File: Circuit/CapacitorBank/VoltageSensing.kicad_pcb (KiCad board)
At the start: 2 copper layers, 48.3 x 22.9 mm, 12 parts, among them J1 From Capacitor Bank, J2 To Control, U1 VTL5C, U2 VTL5C, U3 LM358

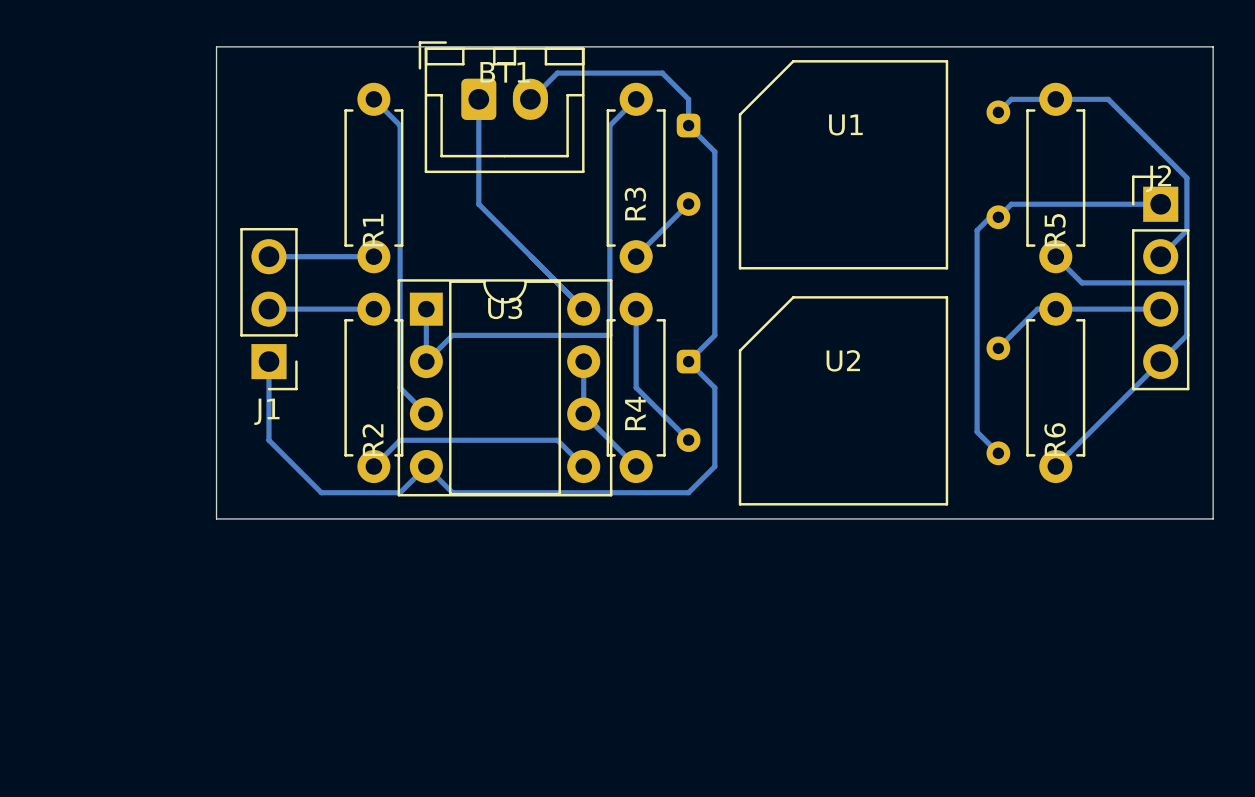
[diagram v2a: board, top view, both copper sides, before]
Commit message: [Circuit] One channel voltage sensing and control modules
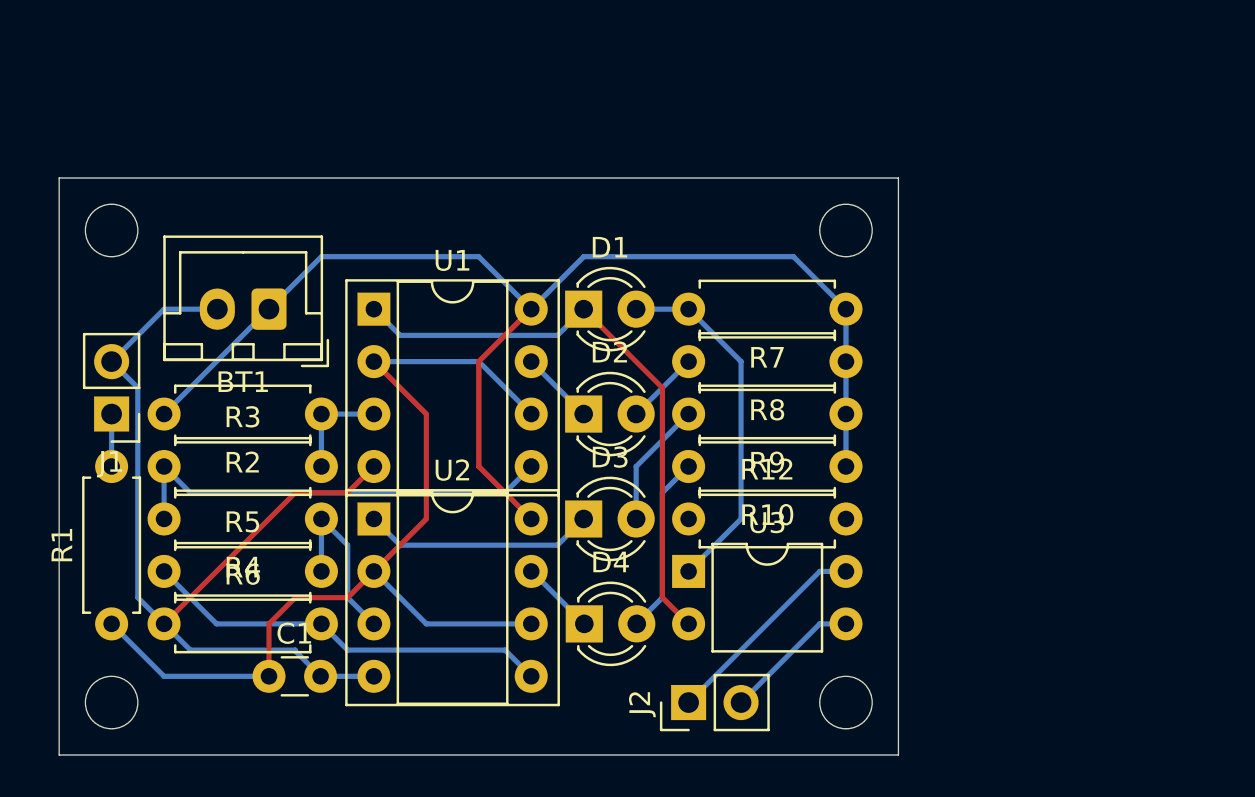
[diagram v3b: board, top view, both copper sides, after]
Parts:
- added C1: 0.1uF, Capacitor_THT:C_Disc_D3.0mm_W1.6mm_P2.50mm, F.Cu at (71.1, 73.7)
- added D1: LED, LED_THT:LED_D3.0mm_FlatTop, F.Cu at (86.4, 55.9)
- added D2: LED, LED_THT:LED_D3.0mm_FlatTop, F.Cu at (86.4, 61.0)
- added D3: LED, LED_THT:LED_D3.0mm_FlatTop, F.Cu at (86.4, 66.0)
- added D4: LED, LED_THT:LED_D3.0mm_FlatTop, F.Cu at (86.4, 71.1)
- added R10: 1K, Resistor_THT:R_Axial_DIN0207_L6.3mm_D2.5mm_P7.62mm_Horizontal, F.Cu at (99.1, 63.5)
- added R12: 1K, Resistor_THT:R_Axial_DIN0207_L6.3mm_D2.5mm_P7.62mm_Horizontal, F.Cu at (91.4, 66.0)
- added R7: 510, Resistor_THT:R_Axial_DIN0207_L6.3mm_D2.5mm_P7.62mm_Horizontal, F.Cu at (99.1, 55.9)
- added R8: 1K, Resistor_THT:R_Axial_DIN0207_L6.3mm_D2.5mm_P7.62mm_Horizontal, F.Cu at (99.1, 58.4)
- added R9: 1K, Resistor_THT:R_Axial_DIN0207_L6.3mm_D2.5mm_P7.62mm_Horizontal, F.Cu at (99.1, 61.0)
- J1: footprint Connector_PinHeader_2.54mm:PinHeader_1x03_P2.54mm_Vertical -> Connector_PinHeader_2.54mm:PinHeader_1x02_P2.54mm_Vertical
- J2: footprint Connector_PinHeader_2.54mm:PinHeader_1x04_P2.54mm_Vertical -> Connector_PinHeader_2.54mm:PinHeader_1x02_P2.54mm_Vertical
- R2: value 1K -> 6.8K
- R3: value 680 -> 5.1K
- R4: value 100 -> 5.1K
- R5, R6: value 4.7K -> 5.1K
- U1, U2: value VTL5C -> LM393; footprint OptoDevice:PerkinElmer_VTL5C -> Package_DIP:DIP-8_W7.62mm_Socket
- U3: value LM358 -> PC817; footprint Package_DIP:DIP-8_W7.62mm_Socket -> Package_DIP:DIP-4_W7.62mm
- moved R5 45.8 mm to (66.0, 68.6), turned to 0 degrees
- moved R6 43.8 mm to (66.0, 71.1), turned to 0 degrees
- moved J2 33.2 mm to (91.4, 74.9), turned to 90 degrees
- moved R1 28.4 mm to (63.5, 71.1), turned to 90 degrees
- moved R3 25.0 mm to (66.0, 63.5), turned to 0 degrees
- moved R4 18.3 mm to (73.7, 66.0), turned to 180 degrees
- moved U3 18.0 mm to (91.4, 68.6)
- moved U1 17.6 mm to (76.2, 55.9)
- moved U2 17.0 mm to (76.2, 66.0)
- moved BT1 14.4 mm to (71.1, 55.9), turned to 180 degrees
- moved J1 8.03 mm to (63.5, 61.0)
- moved R2 3.59 mm to (73.7, 61.0), turned to 180 degrees
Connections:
- J1 pad 1: GND -> /Sensor9V
- J1 pad 2: /Sensor3V -> GND
- J2 pad 1: /ControlPower+ -> /ControlSignal
- J2 pad 2: /ControlSignal1 -> /ControlGND
- R1 pad 1: Net-(R1-Pad1) -> Net-(C1-Pad1)
- R2 pad 2: /Sensor3V -> +12V
- R3 pad 2: Net-(R3-Pad2) -> Net-(R2-Pad1)
- R4 pad 2: Net-(R4-Pad2) -> Net-(R3-Pad1)
- R5 pad 1: /ControlPower- -> Net-(R5-Pad1)
- R5 pad 2: /ControlSignal1 -> Net-(R4-Pad1)
- R6 pad 1: /ControlPower- -> GND
- R6 pad 2: /ControlSignal2 -> Net-(R5-Pad1)
- U1 pad 1: GND -> Net-(D1-Pad1)
- U1 pad 2: Net-(R3-Pad1) -> Net-(C1-Pad1)
- U1 pad 3: /ControlSignal1 -> Net-(R2-Pad1)
- U1 pad 4: /ControlPower+ -> GND
- U2 pad 1: GND -> Net-(D3-Pad1)
- U2 pad 2: Net-(R4-Pad1) -> Net-(C1-Pad1)
- U2 pad 3: /ControlSignal2 -> Net-(R4-Pad1)
- U2 pad 4: /ControlPower+ -> GND
- U3 pad 1: Net-(R3-Pad2) -> Net-(D1-Pad2)
- U3 pad 2: Net-(R3-Pad2) -> Net-(D1-Pad1)
- U3 pad 3: Net-(R1-Pad1) -> /ControlGND
- U3 pad 4: GND -> /ControlSignal
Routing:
- net Net-(C1-Pad1): track 0.00 -> 47.0 mm
- net +12V: track 15.9 -> 59.2 mm
- net Net-(D1-Pad1): track 0.00 -> 28.6 mm
- net Net-(R3-Pad2): track 23.9 -> 0.00 mm
- net /ControlPower+: track 20.6 -> 0.00 mm
- net Net-(R5-Pad1): track 0.00 -> 19.9 mm
- net /ControlPower-: track 18.4 -> 0.00 mm
- net Net-(R3-Pad1): track 3.60 -> 21.4 mm
- net Net-(D1-Pad2): track 0.00 -> 17.3 mm
- net Net-(R1-Pad1): track 16.3 -> 0.00 mm
- net /ControlSignal1: track 15.7 -> 0.00 mm
- net GND: track 56.1 -> 44.5 mm
- net Net-(D3-Pad1): track 0.00 -> 11.2 mm
- net /ControlSignal: track 0.00 -> 10.3 mm
- net Net-(D4-Pad2): track 0.00 -> 8.66 mm
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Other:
- board size 48.3 x 22.9 mm -> 40.6 x 27.9 mm

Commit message: [Circuit] Enable to export gerber files
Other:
- board text added: "M. Gong"
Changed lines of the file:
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@@
   (general
     (thickness 1.6)
-    (drawings 8)
+    (drawings 9)
     (tracks 85)
     (zones 0)
@@
       (creategerberjobfile false)
       (excludeedgelayer true)
-      (linewidth 0.100000)
+      (linewidth 0.250000)
       (plotframeref false)
       (viasonmask false)
@@
       (outputformat 1)
       (mirror false)
-      (drillshape 1)
+      (drillshape 0)
       (scaleselection 1)
-      (outputdirectory ""))
+      (outputdirectory "Gerbers/"))
   )
   (net 0 "")
@@
     )
   )
+  (gr_text "M. Gong" (at 81.28 50.8) (layer F.SilkS)
+    (effects (font (size 1 1) (thickness 0.15)))
+  )
   (gr_circle (center 63.5 52.07) (end 63.5 50.8) (layer Edge.Cuts) (width 0.05))

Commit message: [Circuit] Adjustable delay in control module
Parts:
- U1, U2: footprint Package_DIP:DIP-8_W7.62mm_Socket -> Package_DIP:DIP-8_W7.62mm
- moved J1 2.54 mm to (63.5, 58.4)
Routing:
- net Net-(R4-Pad1): track 8.67 -> 6.13 mm
- net /Sensor9V: track 2.64 -> 5.08 mm
- net GND: track 44.5 -> 45.5 mm
- net Net-(R3-Pad1): track 21.4 -> 20.8 mm

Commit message: [Circuit] Adjust some resistors
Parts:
- R7: value 510 -> 680
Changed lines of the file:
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@@
       (effects (font (size 1 1) (thickness 0.15)))
     )
-    (fp_text value 510 (at 1.27 0) (layer F.Fab)
+    (fp_text value 680 (at 1.27 0) (layer F.Fab)
       (effects (font (size 1 1) (thickness 0.15)))
     )

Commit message: [Circuit] Optimize the interface between capacitor bank modules and voltage sensing module
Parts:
- R2: value 6.8K -> 20K
- R3, R4, R5, R6: value 5.1K -> 4.7K
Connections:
- net /Sensor9V renamed /Sensor6V

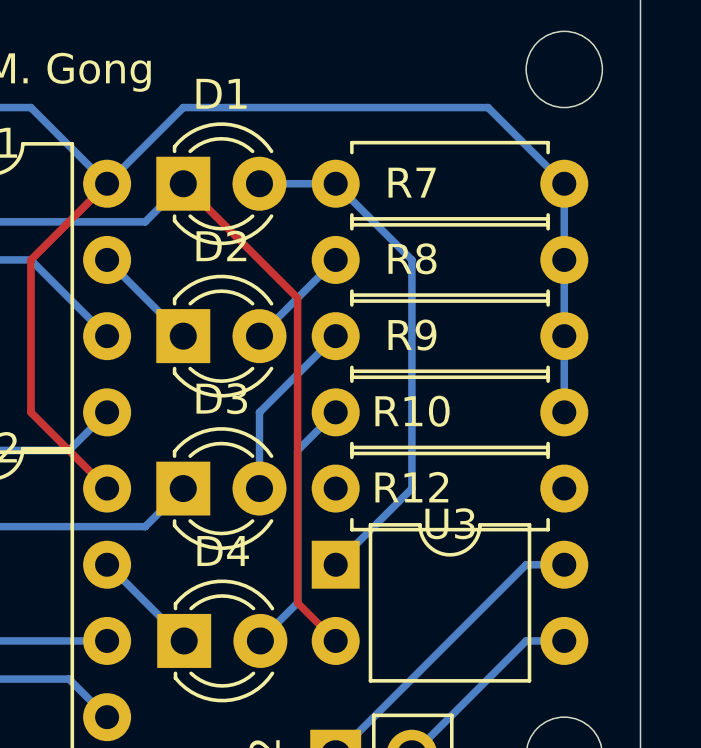
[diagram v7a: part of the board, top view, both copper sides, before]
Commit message: [Circuit] Fix the resistors in voltage sensing module
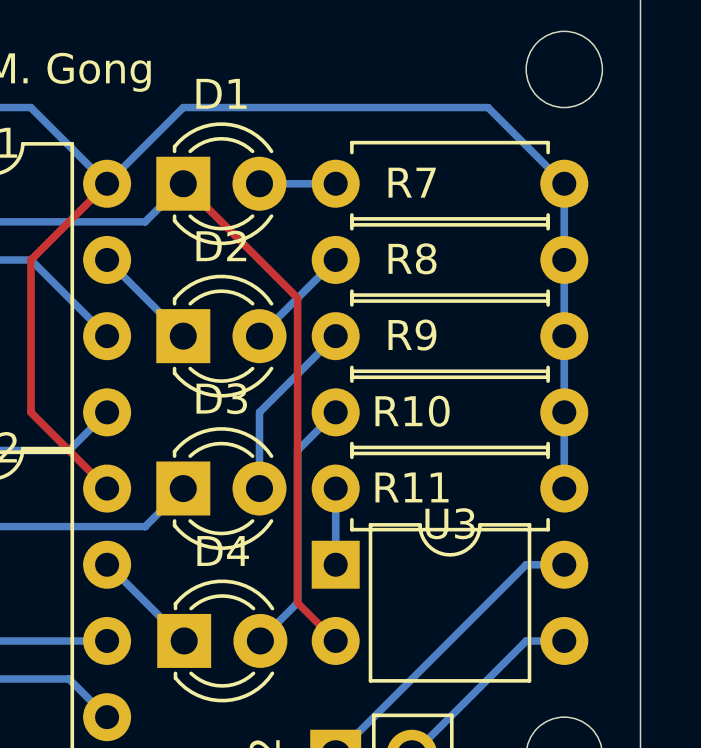
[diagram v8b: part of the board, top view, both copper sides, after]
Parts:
- removed R12: 1K, Resistor_THT:R_Axial_DIN0207_L6.3mm_D2.5mm_P7.62mm_Horizontal
- added R11: 1K, Resistor_THT:R_Axial_DIN0207_L6.3mm_D2.5mm_P7.62mm_Horizontal, F.Cu at (99.1, 66.0)
- R10, R8, R9: value 1K -> 2.2K
- R7: value 680 -> 2.2K
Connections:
- U3 pad 1: Net-(D1-Pad2) -> Net-(R11-Pad2)
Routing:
- net Net-(D1-Pad2): track 17.3 -> 2.54 mm
- net +12V: track 59.2 -> 61.8 mm
- net Net-(R11-Pad2): track 0.00 -> 2.54 mm
